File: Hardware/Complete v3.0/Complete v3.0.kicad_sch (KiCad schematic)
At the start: 221 parts, among them Q1 SI2301DS, U1 TPS7A0230PDBVR, U2 ATMEGA4808-AU, U3 DS3231MZ_

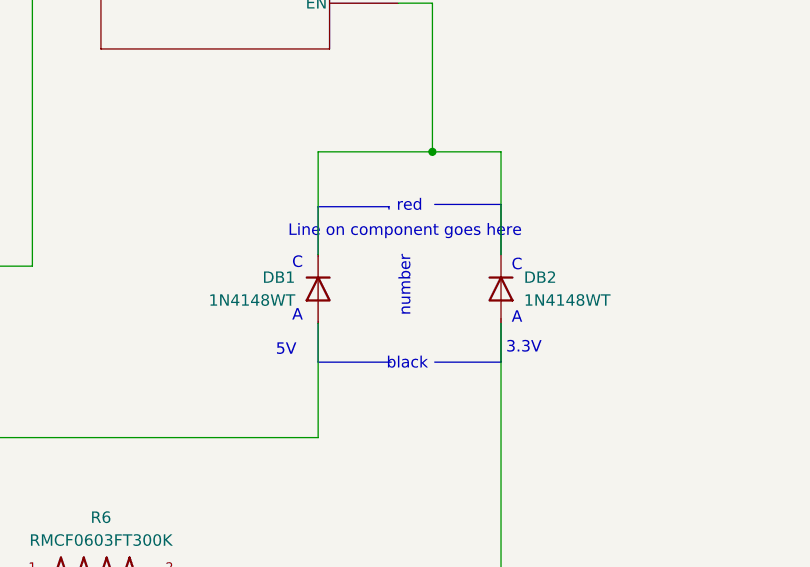
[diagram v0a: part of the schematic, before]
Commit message: Version 3 software update
• set the BOD to 2.6V (dont go higher than that)

• Added charger wake flag

• Added charger indicator

• Set the software version number to match the hardware number
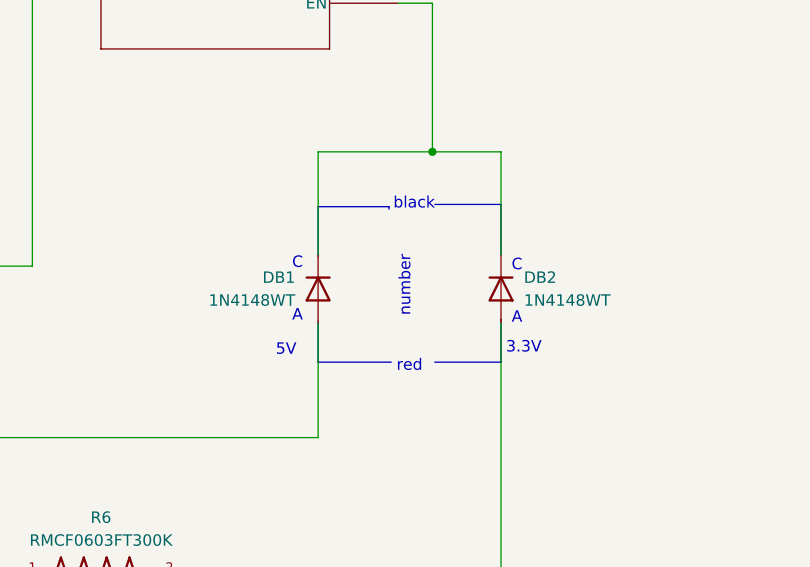
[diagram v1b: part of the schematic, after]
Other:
- note removed: "Line on component goes here"
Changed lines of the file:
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@@
 	(text "black\n"
 		(exclude_from_sim no)
-		(at 221.996 84.582 0)
+		(at 222.758 66.802 0)
 		(effects
 			(font
@@
 			(font
 				(size 3.81 3.81)
-			)
-		)
-	)
-	(text "Line on component goes here"
-		(exclude_from_sim no)
-		(at 221.742 69.85 0)
-		(effects
-			(font
-				(size 1.27 1.27)
 			)
 		)
@@
 	(text "red"
 		(exclude_from_sim no)
-		(at 222.25 67.056 0)
+		(at 222.25 84.836 0)
 		(effects
 			(font

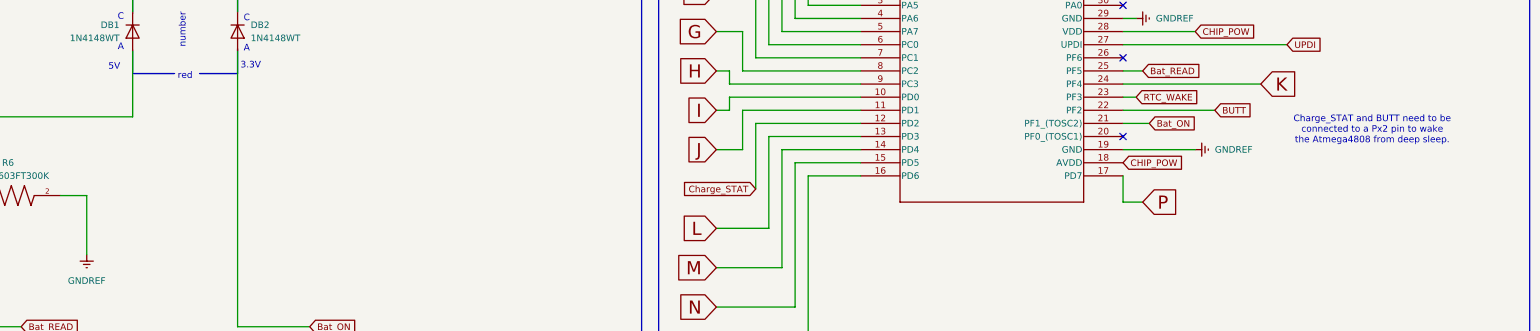
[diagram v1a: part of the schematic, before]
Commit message: Near Final Update
Found out the BOD controller only shuts down the chip control instead of shutting down the functionality of the pins. I have rewrote the software to use a different control function (VLM instead of BOD) so it should (in theory) be able to shut down safely.

Additionally, I re-wired 2 traces on the circuit board so that the battery-percentage module is 100% safe and will not drain the battery. It's not worth paying the money to get new boards printed, since there's only one non-critical wire added to the back of the board. If the wire breaks contact, the battery read module will read 99% since there's no "ground" connected.

This needs to be tested, of course.
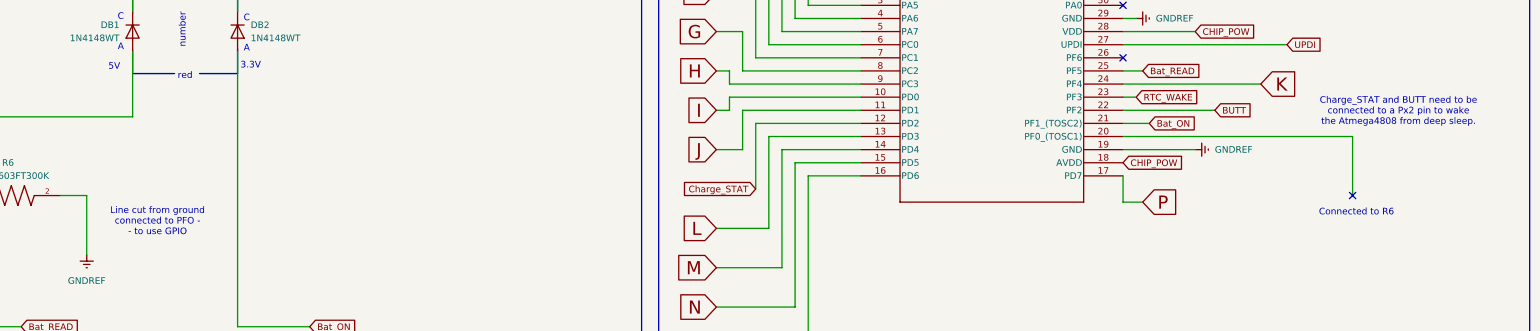
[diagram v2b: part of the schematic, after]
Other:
- note added: "Connected to R6"
- note added: "Line cut from ground connected to PFO - - to use GPIO"
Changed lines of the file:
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@@
 	(text "Charge_STAT and BUTT need to be \nconnected to a Px2 pin to wake\nthe Atmega4808 from deep sleep."
 		(exclude_from_sim no)
-		(at 452.12 95.25 0)
+		(at 457.2 91.694 0)
 		(effects
 			(font
@@
 		)
 	)
+	(text "Line cut from ground\nconnected to PFO - \n- to use GPIO"
+		(exclude_from_sim no)
+		(at 216.916 113.03 0)
+		(effects
+			(font
+				(size 1.27 1.27)
+			)
+		)
+	)
 	(text "number"
 		(exclude_from_sim no)
@@
 		)
 	)
+	(text "Connected to R6"
+		(exclude_from_sim no)
+		(at 449.072 111.252 0)
+		(effects
+			(font
+				(size 1.27 1.27)
+			)
+		)
+	)
 	(text "drain"
 		(exclude_from_sim no)
@@
 	)
 	(no_connect
-		(at 403.86 96.52)
+		(at 448.31 107.95)
 	)
 	(no_connect
@@
 	(wire
 		(pts
+			(xy 403.86 96.52) (xy 448.31 96.52)
+		)
+		(stroke
+			(width 0)
+			(type default)
+		)
+	)
+	(wire
+		(pts
 			(xy 186.69 266.7) (xy 179.07 266.7)
 		)
@@
 		)
 		(stroke
+			(width 0)
+			(type default)
+		)
+	)
+	(wire
+		(pts
+			(xy 448.31 96.52) (xy 448.31 107.95)
+		)
+		(stroke
